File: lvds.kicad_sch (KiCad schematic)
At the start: 102 parts, among them J15 Conn_FFC_Amphenol_62684-40210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, U1 TLV76701_WSON6

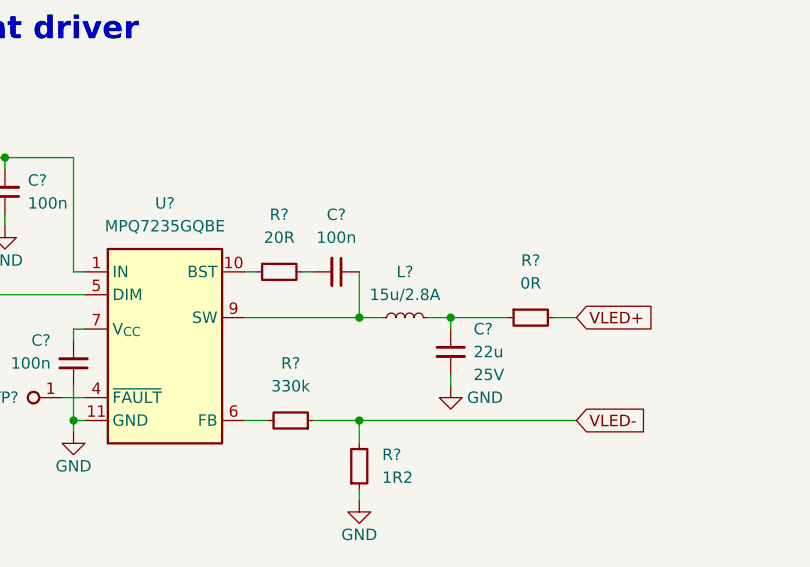
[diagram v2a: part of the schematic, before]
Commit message: [#54932] Change backlight driver inductor to smaller one
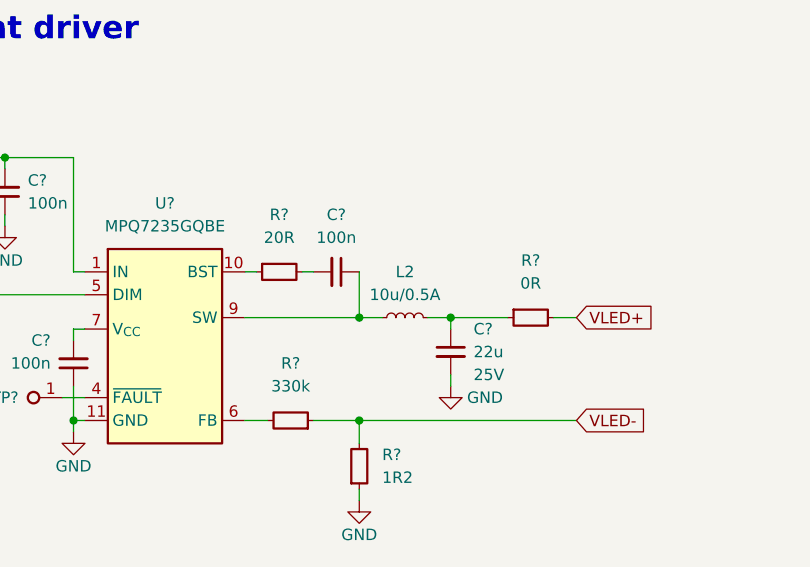
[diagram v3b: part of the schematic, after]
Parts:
- removed L?: L_15u_2.8A_Coilcraft-XAL4040, antmicro-footprints:L_Coilcraft-XAL4040, symbol antmicroFixedInductors:L_15u_2.8A_Coilcraft-XAL4040
- added L2: L_10u_0.5A_Murata-8200, antmicro-footprints:L_Murata-8200, symbol antmicroFixedInductors:L_10u_0.5A_Murata-8200
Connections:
- net at C?.1, U?.9 (SW): now also L2.1
- net at C?.1, R?.1: now also L2.2
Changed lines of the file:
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@@
     )
   )
-  (symbol (lib_id "antmicroFixedInductors:L_15u_2.8A_Coilcraft-XAL4040") (at 220.98 213.36 0) (unit 1)
-    (in_bom yes) (on_board yes) (dnp no) (fields_autoplaced)
-    (property "Reference" "L?" (at 223.52 208.28 0)
-      (effects (font (size 1.27 1.27) (thickness 0.15)))
-    )
-    (property "Value" "L_15u_2.8A_Coilcraft-XAL4040" (at 236.22 223.52 0)
-      (effects (font (size 1.27 1.27) (thickness 0.15)) (justify left bottom) hide)
-    )
-    (property "Footprint" "antmicro-footprints:L_Coilcraft-XAL4040" (at 236.22 226.06 0)
-      (effects (font (size 1.27 1.27) (thickness 0.15)) (justify left bottom) hide)
-    )
-    (property "Datasheet" "https://www.coilcraft.com/getmedia/6adcb47d-8b55-416c-976e-1e22e0d2848c/xal4000.pdf" (at 236.22 228.6 0)
-      (effects (font (size 1.27 1.27) (thickness 0.15)) (justify left bottom) hide)
-    )
-    (property "Manufacturer" "Coilcraft" (at 236.22 231.14 0)
-      (effects (font (size 1.27 1.27) (thickness 0.15)) (justify left bottom) hide)
-    )
-    (property "MPN" "XAL4040-153" (at 236.22 233.68 0)
-      (effects (font (size 1.27 1.27) (thickness 0.15)) (justify left bottom) hide)
-    )
-    (property "ISat" "2.9 A" (at 236.22 236.22 0)
-      (effects (font (size 1.27 1.27) (thickness 0.15)) (justify left bottom) hide)
-    )
-    (property "IMax" "2.8 A" (at 236.22 238.76 0)
-      (effects (font (size 1.27 1.27) (thickness 0.15)) (justify left bottom) hide)
-    )
-    (property "Size" "4.0x4.0" (at 236.22 241.3 0)
-      (effects (font (size 1.27 1.27) (thickness 0.15)) (justify left bottom) hide)
-    )
-    (property "Val" "15u/2.8A" (at 223.52 210.82 0)
-      (effects (font (size 1.27 1.27) (thickness 0.15)))
-    )
-    (property "Author" "Antmicro" (at 236.22 243.84 0)
-      (effects (font (size 1.27 1.27) (thickness 0.15)) (justify left bottom) hide)
-    )
-    (property "License" "Apache-2.0" (at 236.22 246.38 0)
-      (effects (font (size 1.27 1.27) (thickness 0.15)) (justify left bottom) hide)
-    )
-    (pin "1")
-    (pin "2")
-    (instances
-      (project "cm4-lvds-adapter"
-        (path "/60b842dc-0853-4a25-99ac-5784ddf94d0d/08a1e442-f0a3-4779-ba71-f71979b0fc7c"
-          (reference "L?") (unit 1)
-        )
-      )
-    )
-  )
   (symbol (lib_id "antmicroCapacitors0402:C_1u_0402") (at 214.63 82.55 90) (unit 1)
     (in_bom yes) (on_board yes) (dnp no) (fields_autoplaced)
@@
         )
       )
+    )
+  )
+  (symbol (lib_id "antmicroFixedInductors:L_10u_0.5A_Murata-8200") (at 220.98 213.36 0) (unit 1)
+    (in_bom yes) (on_board yes) (dnp no) (fields_autoplaced)
+    (property "Reference" "L2" (at 223.52 208.28 0)
+      (effects (font (size 1.27 1.27) (thickness 0.15)))
+    )
+    (property "Value" "L_10u_0.5A_Murata-8200" (at 234.95 215.9 0)
+      (effects (font (size 1.27 1.27) (thickness 0.15)) (justify left bottom) hide)
+    )
+    (property "Footprint" "antmicro-footprints:L_Murata-8200" (at 234.95 220.98 0)
+      (effects (font (size 1.27 1.27) (thickness 0.15)) (justify left bottom) hide)
+    )
+    (property "Datasheet" "https://www.murata-ps.com/data/magnetics/kmp_8200c.pdf" (at 234.95 223.52 0)
+      (effects (font (size 1.27 1.27) (thickness 0.15)) (justify left bottom) hide)
+    )
+    (property "Val" "10u/0.5A" (at 223.52 210.82 0)
+      (effects (font (size 1.27 1.27) (thickness 0.15)))
+    )
+    (property "Manufacturer" "Murata" (at 234.95 226.06 0)
+      (effects (font (size 1.27 1.27) (thickness 0.15)) (justify left bottom) hide)
+    )
+    (property "MPN" "82103C" (at 234.95 228.6 0)
+      (effects (font (size 1.27 1.27) (thickness 0.15)) (justify left bottom) hide)
+    )
+    (property "ISat" "" (at 234.95 229.87 0)
+      (effects (font (size 1.27 1.27)) (justify left) hide)
+    )
+    (property "IMax" "0.5A" (at 234.95 233.68 0)
+      (effects (font (size 1.27 1.27) (thickness 0.15)) (justify left bottom) hide)
+    )
+    (property "Size" "3.20x2.50" (at 234.95 236.22 0)
+      (effects (font (size 1.27 1.27) (thickness 0.15)) (justify left bottom) hide)
+    )
+    (property "Author" "Antmicro" (at 234.95 238.76 0)
+      (effects (font (size 1.27 1.27) (thickness 0.15)) (justify left bottom) hide)
+    )
+    (property "License" "Apache-2.0" (at 234.95 241.3 0)
+      (effects (font (size 1.27 1.27) (thickness 0.15)) (justify left bottom) hide)
+    )
+    (pin "2")
+    (pin "1")
+    (instances
+      (project "cm4-lvds-adapter"
+        (path "/60b842dc-0853-4a25-99ac-5784ddf94d0d/08a1e442-f0a3-4779-ba71-f71979b0fc7c"
+          (reference "L2") (unit 1)
+        )
+      )

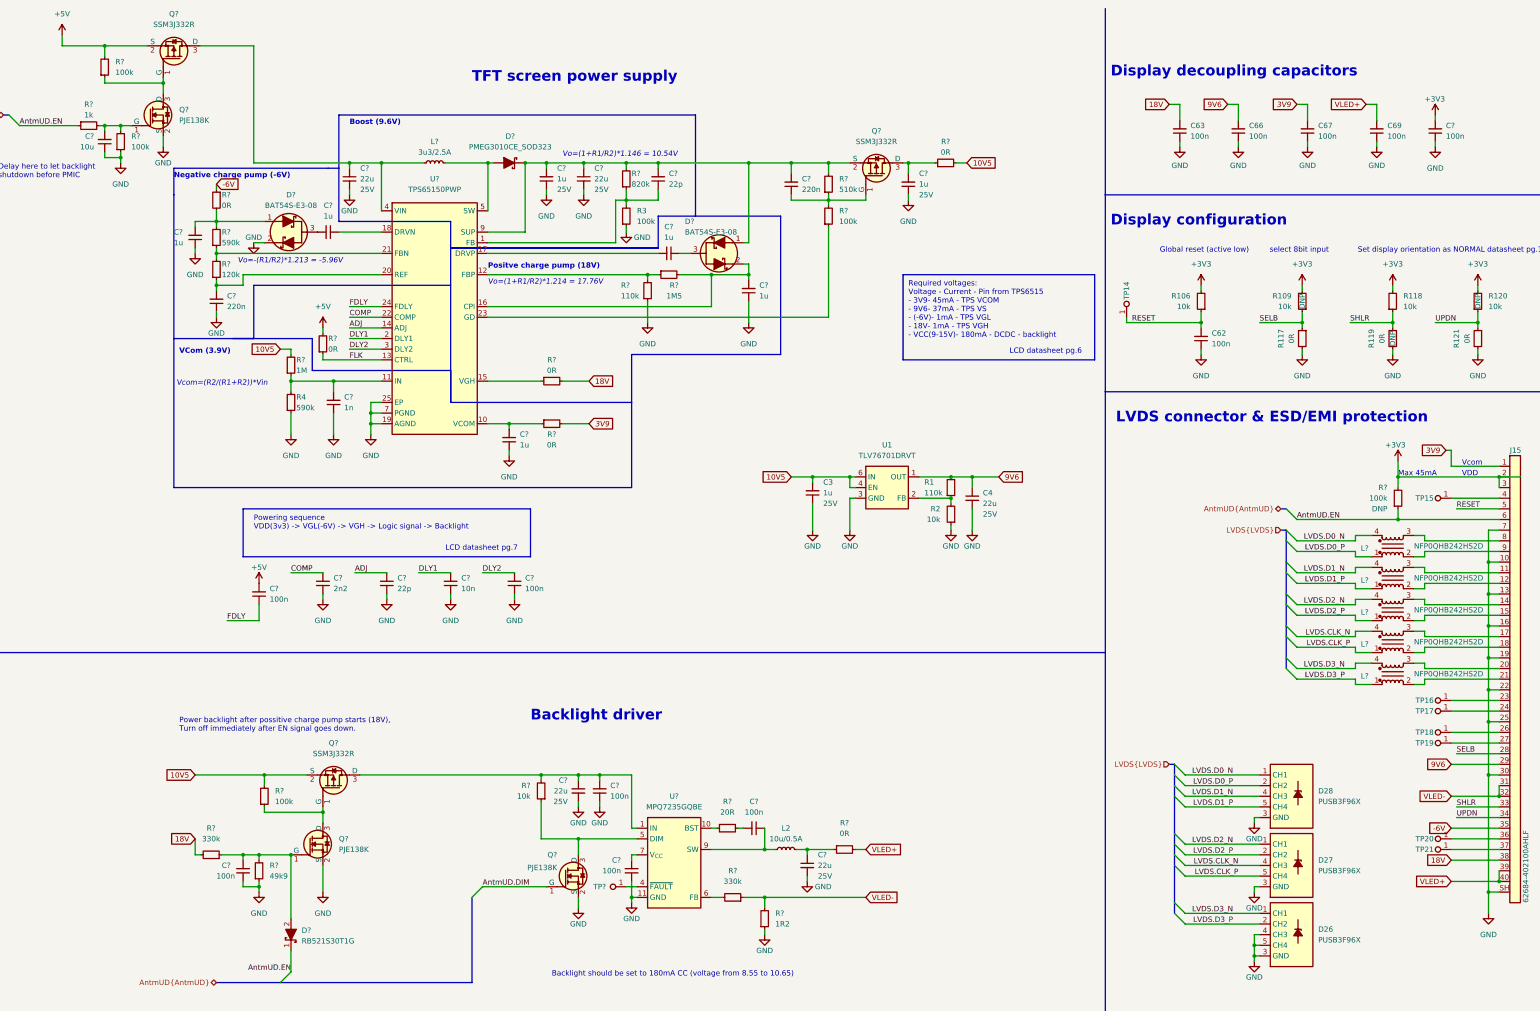
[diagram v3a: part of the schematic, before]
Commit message: [#54932] Reanotate schematics; Propagate component changes to PCB
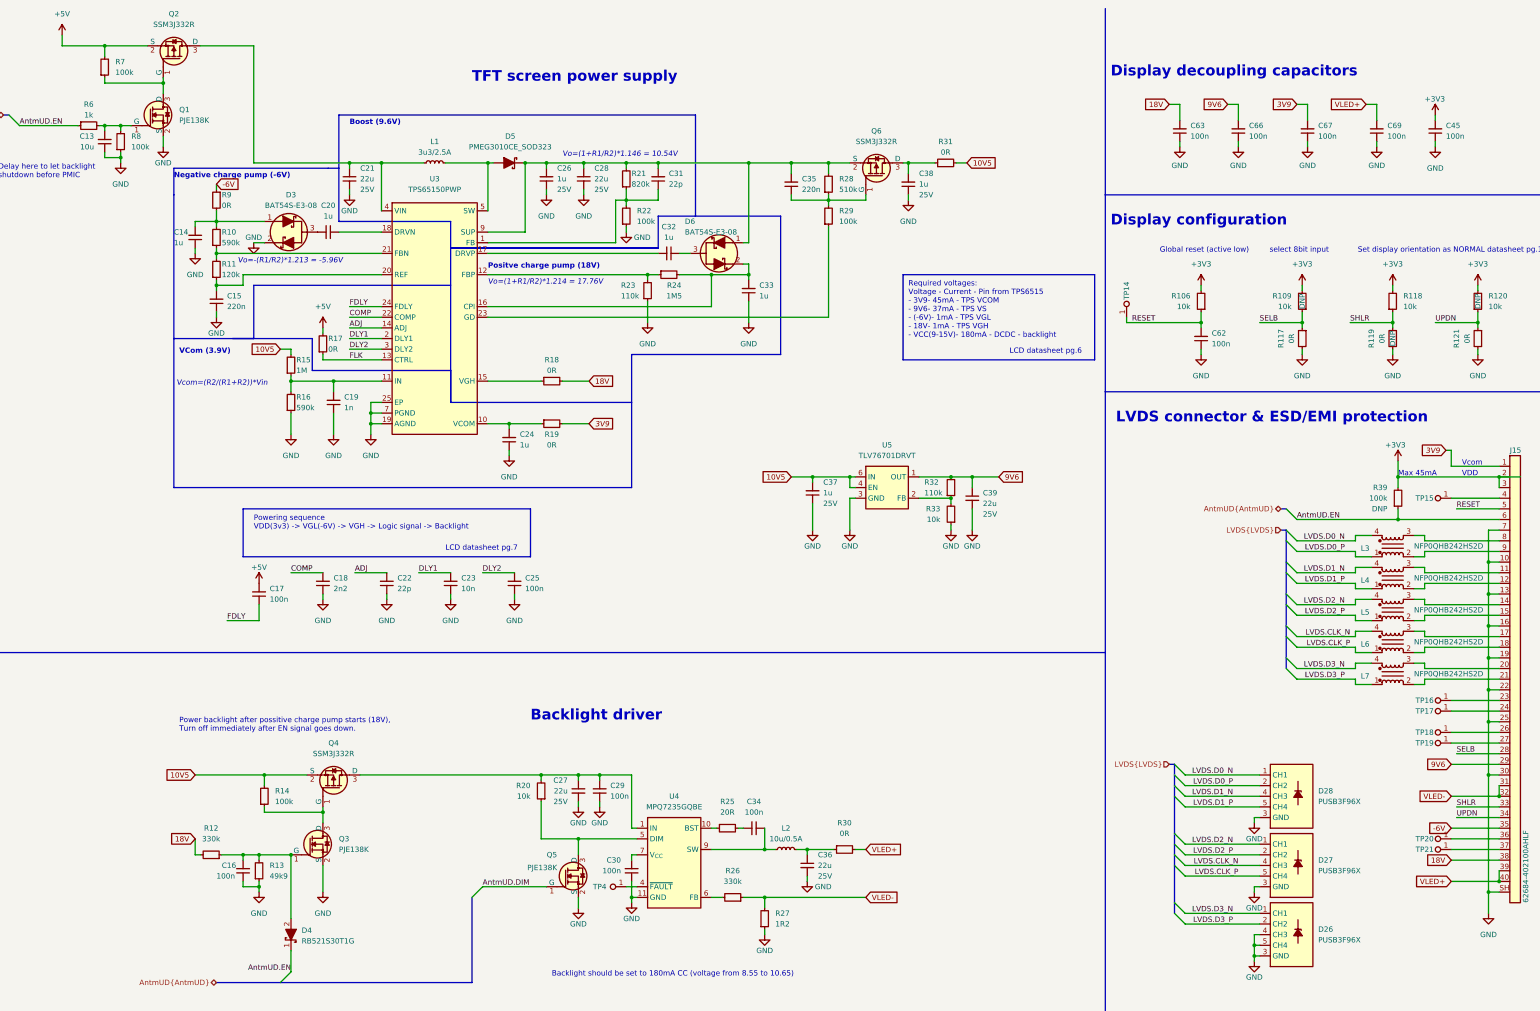
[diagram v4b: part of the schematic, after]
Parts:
- gave numbers to parts that had none: 70
- renumbered C3 to C37, C4 to C39, R4 to R16, R3 to R22, R1 to R32, R2 to R33, U1 to U5
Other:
- title: CM4 Baseboard -> CM4 Baseboard LVDS Adapter

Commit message: [#54932] Reanotate schematics
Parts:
- renumbered C13 to C15, C14 to C16, C15 to C17, C16 to C18, C17 to C19, C18 to C20, C19 to C21, C20 to C22, C21 to C23, C22 to C24, C23 to C25, C24 to C26, C25 to C27, C26 to C28, C27 to C29, C28 to C30, C29 to C31, C30 to C32, C31 to C33, C32 to C34, C33 to C35, C34 to C36, C35 to C37, C36 to C38, C37 to C39, C38 to C40, C39 to C41, C45 to C47, U3 to U4, U4 to U5, U5 to U6

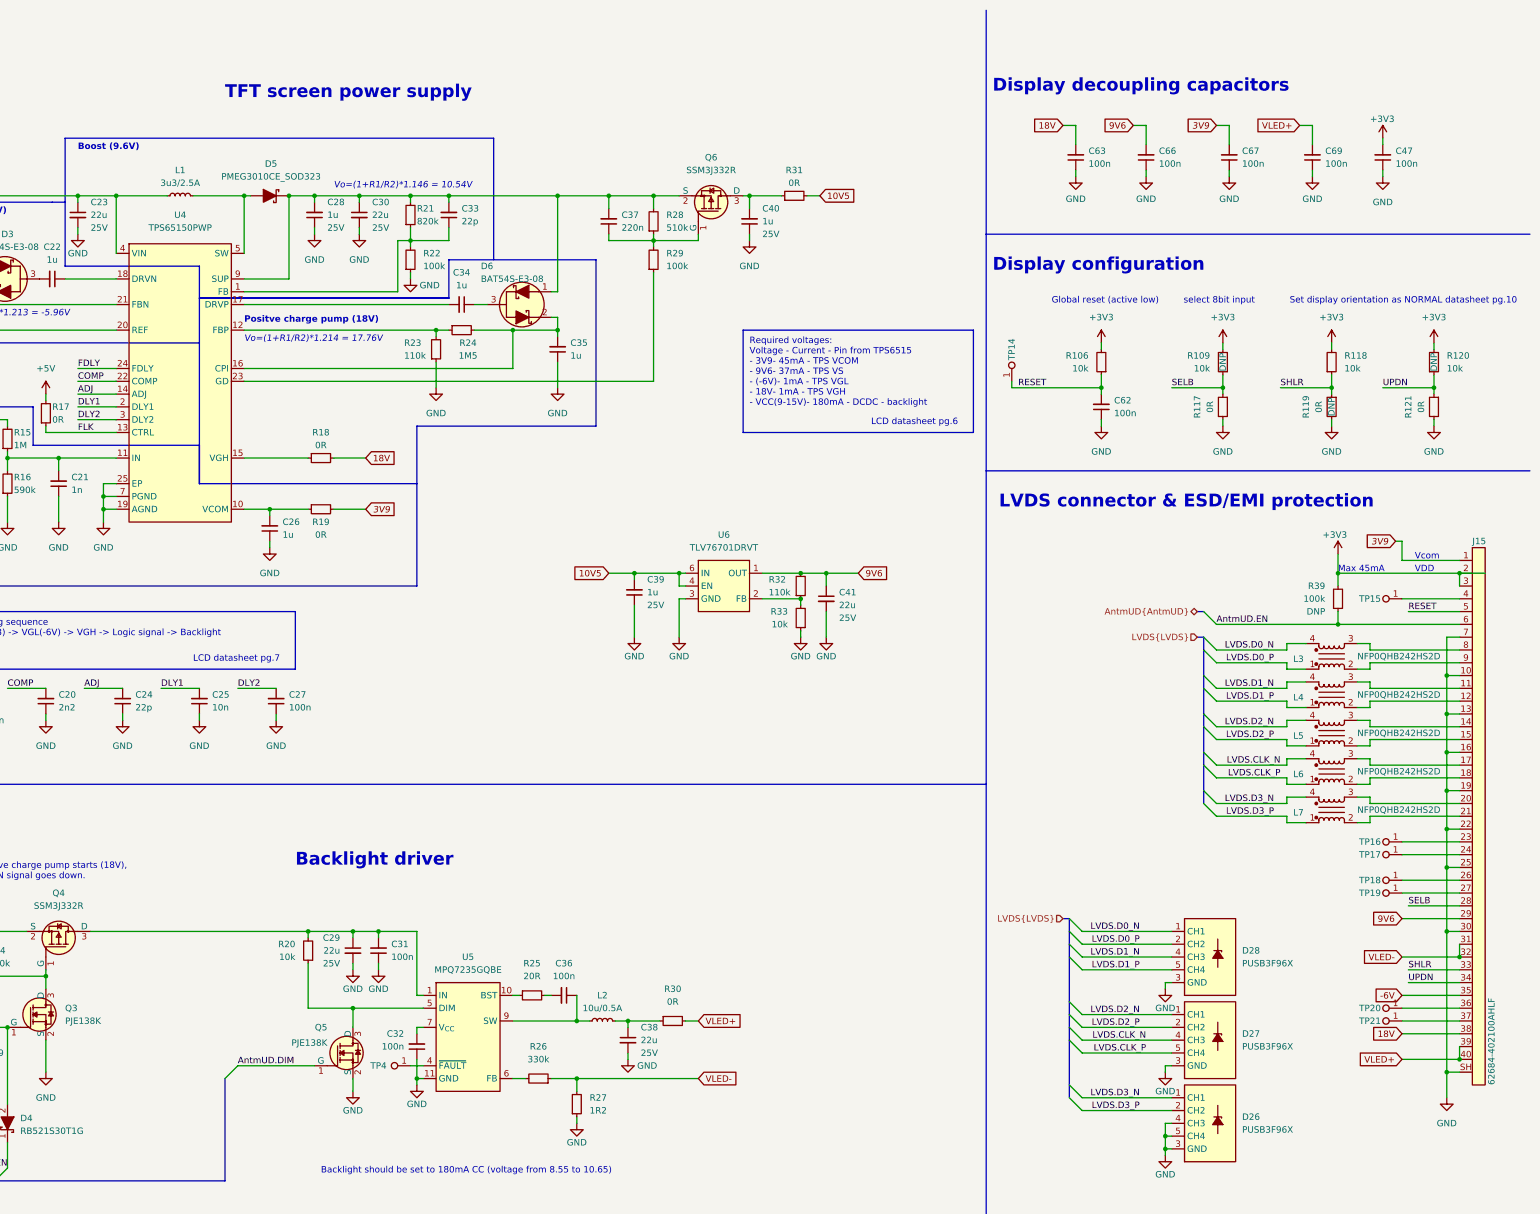
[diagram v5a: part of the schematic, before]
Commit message: [#54932] Add power indicators
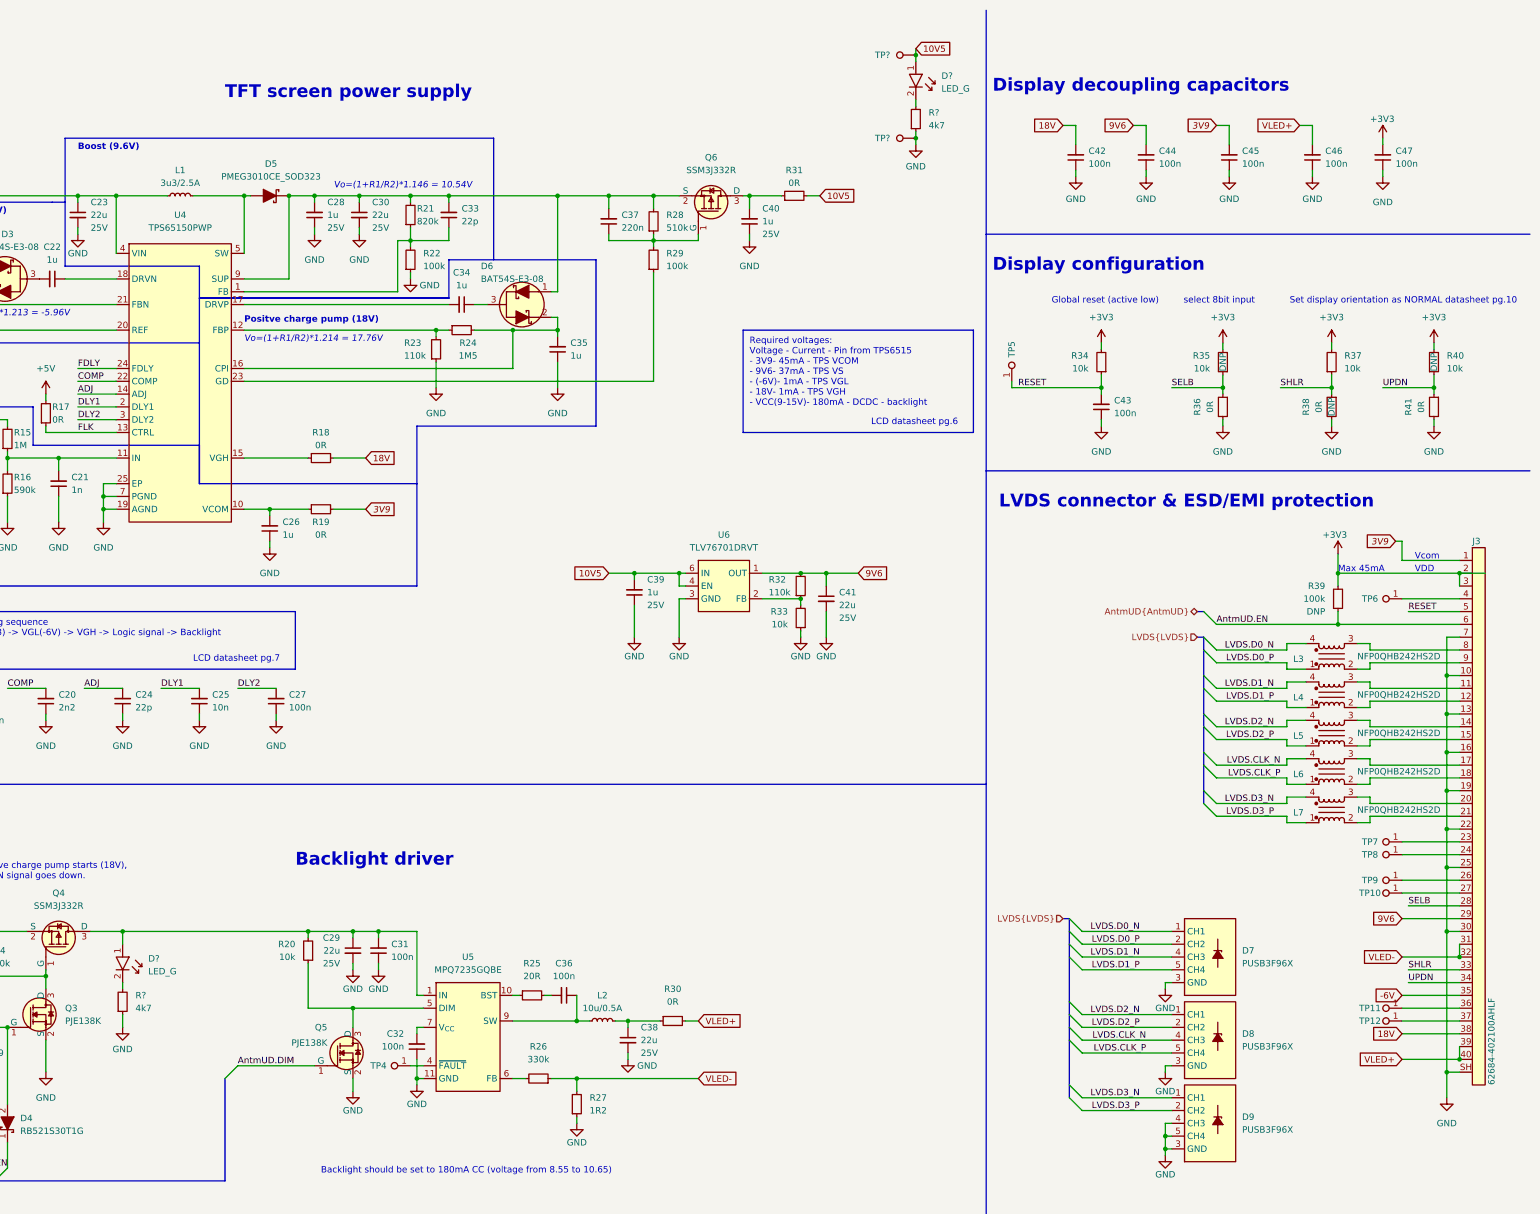
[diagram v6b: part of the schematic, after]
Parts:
- added D? (x2): LED_G, antmicro-footprints:LED_0603_1608Metric_R, symbol antmicroLEDIndicationDiscrete:LED_R_0603_598-8D80-107F
- added R? (x2): R_4k7_0402, antmicro-footprints:R_0402_1005Metric, symbol antmicroResistors0402:R_4k7_0402
- added TP? (x2): TP_1mm_SMD, antmicro-footprints:TP_SMD_1mm, symbol antmicroTestPoints:TP_1mm_SMD
- renumbered C63 to C42, C62 to C43, C66 to C44, C67 to C45, C69 to C46, D28 to D7, D27 to D8, D26 to D9, J15 to J3, R106 to R34, R109 to R35, R117 to R36, R118 to R37, R119 to R38, R120 to R40, R121 to R41, TP19 to TP10, TP20 to TP11, TP21 to TP12, TP14 to TP5, TP15 to TP6, TP16 to TP7, TP17 to TP8, TP18 to TP9
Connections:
- net 10V5: now also D?.1, TP?.1
- net GND: now also R?.1, R?.1, TP?.1
- net at C29.1, C31.2, Q4.3 (D)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: now also D?.1
- new net: D?.2, R?.2 (x2)

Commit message: [#54932] Reanotate schematics
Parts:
- gave numbers to parts that had none: 6
- renumbered D6 to D10, D7 to D12, D8 to D13, D9 to D14, D3 to D6, D4 to D7, D5 to D9, Q1 to Q2, Q2 to Q3, Q3 to Q4, Q4 to Q5, Q5 to Q6, Q6 to Q7, R7 to R10, R8 to R11, R9 to R12, R10 to R13, R11 to R14, R12 to R15, R13 to R16, R14 to R17, R15 to R18, R16 to R19, R17 to R20, R18 to R22, R19 to R23, R20 to R24, R21 to R25, R22 to R26, R23 to R27, R24 to R28, R25 to R29, R26 to R30, R27 to R31, R28 to R32, R29 to R33, R30 to R34, R31 to R35, R32 to R36, R33 to R37, R34 to R39, R35 to R40, R36 to R41, R37 to R42, R38 to R43, R39 to R44, R40 to R45, R41 to R46, R6 to R9, TP4 to TP10, TP5 to TP13, TP6 to TP14, TP7 to TP15, TP8 to TP16, TP9 to TP17, TP10 to TP18, TP11 to TP19, TP12 to TP20
